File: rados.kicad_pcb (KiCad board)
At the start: 2 copper layers, 83.6 x 106.1 mm, 163 parts, among them J1 CONN_02X03, J10 STEPSTICK, J11 STEPSTICK, J12 STEPSTICK, J13 MICROSD_SLOT_TFP09-2-12B, J2 CONN_02X03, J3 CONN_02X03, J4 STEPSTICK, J5 STEPSTICK, J6 STEPSTICK, J7 CONN_02X03, J8 CONN_02X03, J9 CONN_02X03, P1 CONN_01X02, P10 CONN_01X04, P11 CONN_01X04, P12 CONN_01X04, P13 CONN_02x05, P14 CONN_02x05, P15 CONN_02x07, P16 CONN_01X07, P17 CONN_01X03, P18 CONN_01X03, P19 CONN_01X03, P2 CONN_01X02, P20 CONN_01X03, P21 CONN_02x05, P23 CONN_01X02, P24 CONN_01X02, P25 CONN_01X03, P3 CONN_01X02, P4 CONN_01X02, P5 TERMINAL_BLOCK, P6 TERMINAL_BLOCK, P7 CONN_02X04, P8 CONN_01X04, P9 CONN_01X04, Q1 2N7002P, Q10 2N7002P, Q11 2N7002P, Q12 BC846BPDW1, Q13 BC846BPDW1, Q14 SI2318CDS-T1-GE3, Q15 IRFB7545PbF, Q16 2N7002P, Q17 2N7002P, Q18 BC846BPDW1, Q19 BC846BPDW1, Q2 2N7002P, Q20 SI2318CDS-T1-GE3, Q21 IRFB7545PbF, Q3 2N7002P, Q4 BC846BPDW1, Q5 BC846BPDW1, Q6 BC846BPDW1, Q7 IRFB7545PbF, Q8 SI2318CDS-T1-GE3, Q9 IRFB7545PbF, SW1 BUTTON, U1 ST1S14PHR, U3 ESP-12E

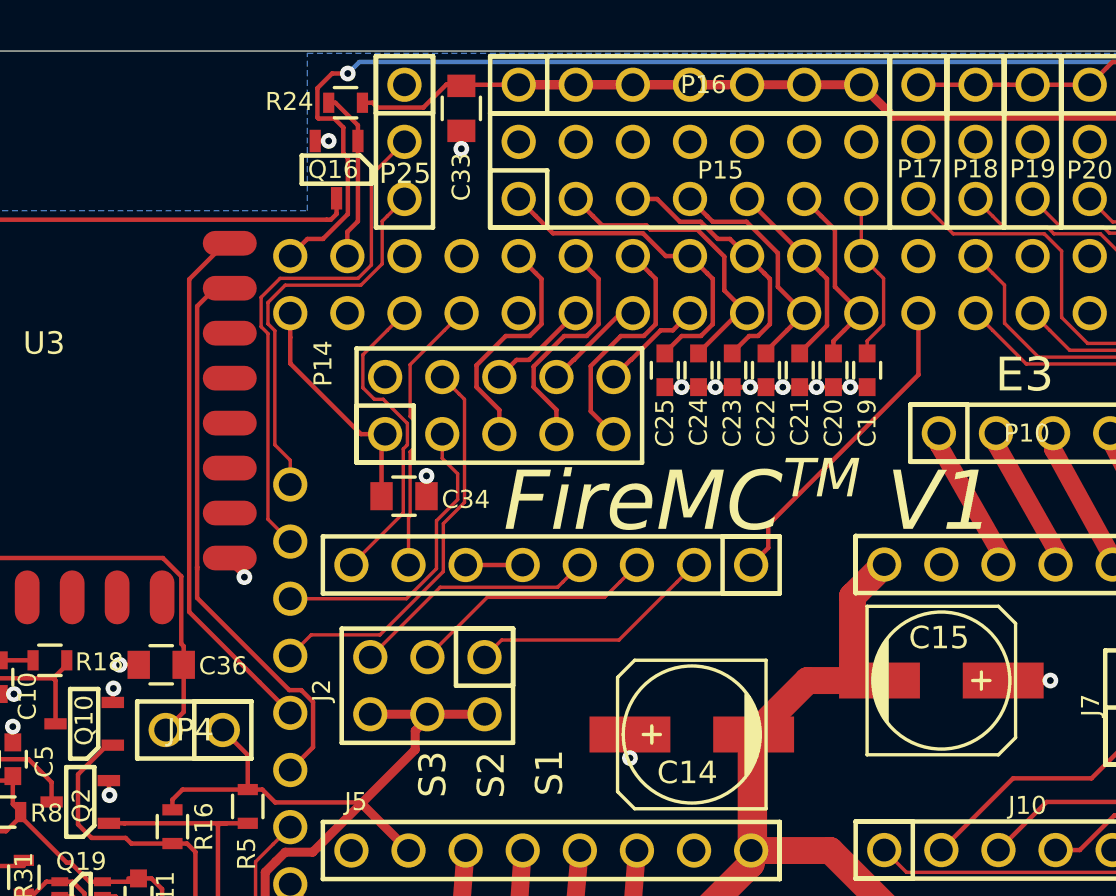
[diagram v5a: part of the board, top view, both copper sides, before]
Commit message: Clearance around wifi power jumper
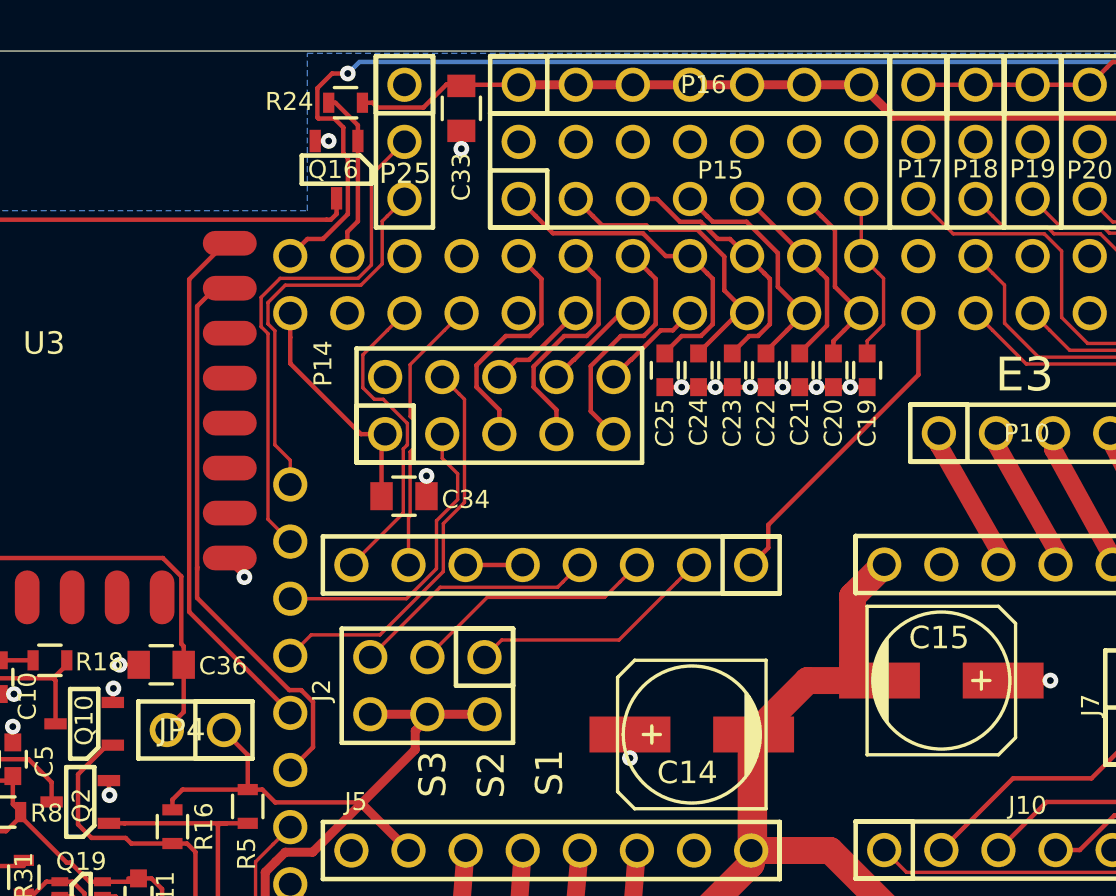
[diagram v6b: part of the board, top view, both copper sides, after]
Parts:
- removed G***: LOGO, logos:OSHW-LOGO
- removed svg2mod (x2): G***, logos:firemc-logo
- removed svg2mod: G***, logos:OtherUseLogo_medium
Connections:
- net Net-(SHIELD1-Pad3V3) renamed Vbuffer
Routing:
- net +3V3: track 474.4 -> 465.9 mm

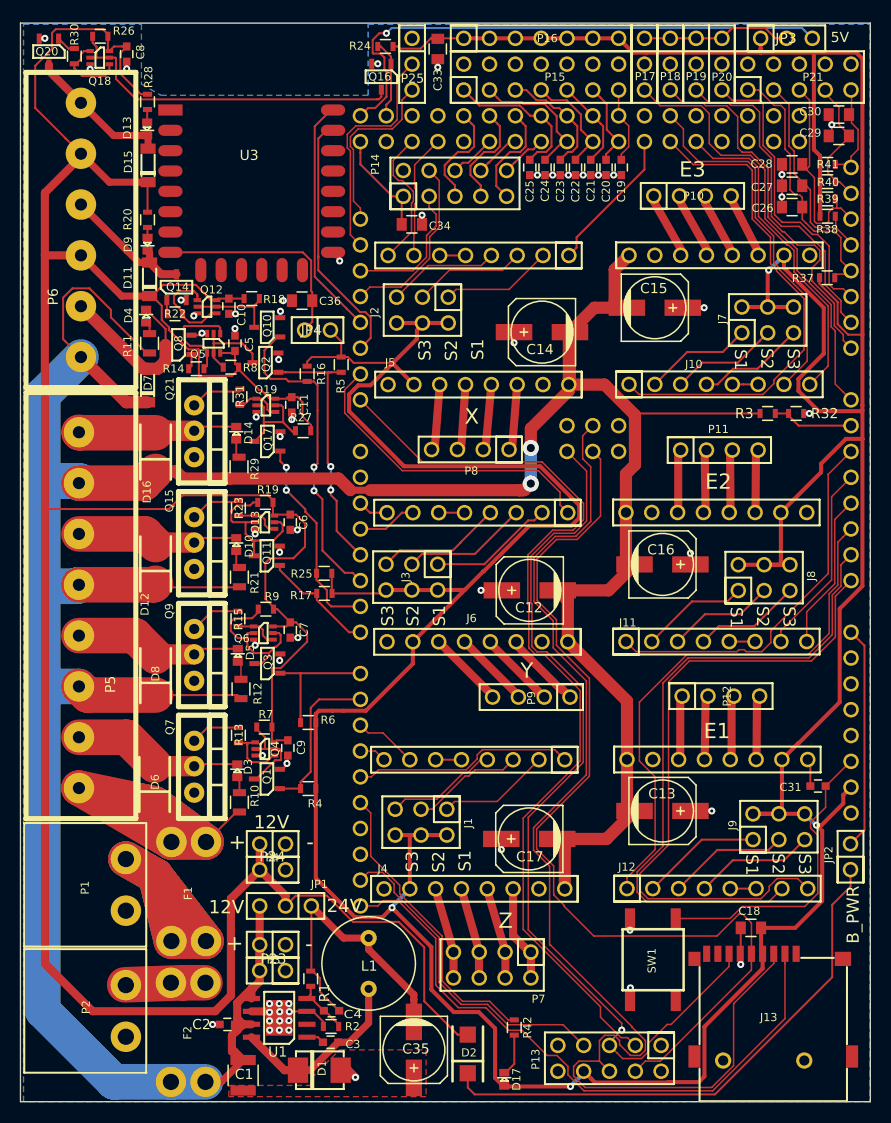
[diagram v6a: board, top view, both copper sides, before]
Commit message: fix analog and wifi
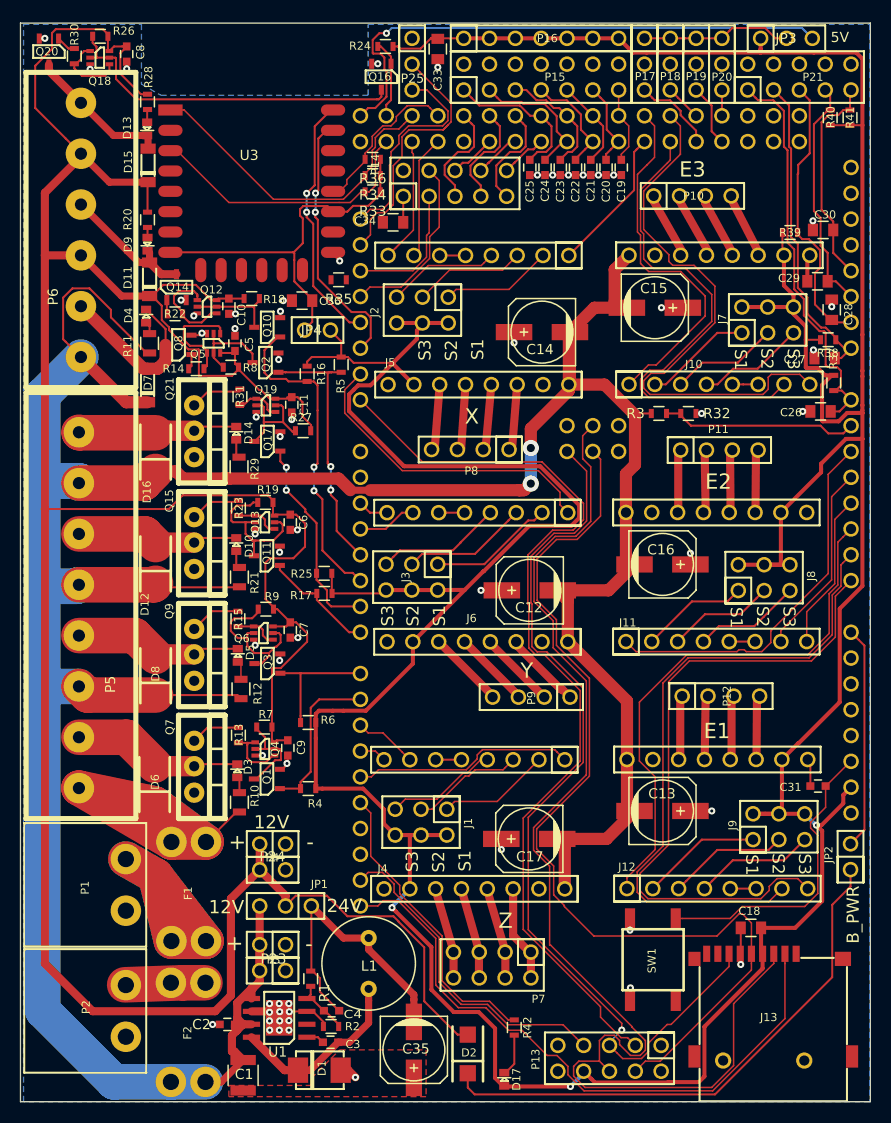
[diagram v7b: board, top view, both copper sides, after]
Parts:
- added R33: 10K, resistors:R_0603, F.Cu at (105.3, 40.5)
- added R34: 10K, resistors:R_0603, F.Cu at (105.3, 38.9)
- added R35: 10K, resistors:R_0603, F.Cu at (102.0, 49.1)
- added R36: 10K, resistors:R_0603, F.Cu at (105.3, 37.3)
- moved C26 20.3 mm to (149.4, 62.1)
- moved C27 17.2 mm to (149.8, 56.9)
- moved C28 14.8 mm to (150.5, 52.1), turned to 90 degrees
- moved C29 14.5 mm to (149.1, 49.3)
- moved R38 12.2 mm to (150.2, 55.0)
- moved C30 11.5 mm to (149.7, 44.2)
- moved R3 10.7 mm to (133.5, 62.3)
- moved R32 10.6 mm to (136.4, 62.3)
- moved R37 10.4 mm to (150.7, 59.3), turned to 270 degrees
- moved R40 6.30 mm to (150.3, 33.2), turned to 90 degrees
- moved R41 5.10 mm to (152.3, 33.2), turned to 90 degrees
- moved R39 4.96 mm to (146.4, 44.5)
- moved C34 1.86 mm to (107.3, 43.5), turned to 180 degrees
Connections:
- C36 pad 1: Net-(C36-Pad1) -> Vesp
- JP4 pad 2: Net-(C36-Pad1) -> Vesp
- SHIELD1 pad 22: Net-(SHIELD1-Pad22) -> ESP-PD
- SHIELD1 pad 25: Net-(SHIELD1-Pad25) -> ESP-RST
- SHIELD1 pad 27: Net-(SHIELD1-Pad27) -> ESP-PROG
- SHIELD1 pad 43: Net-(SHIELD1-Pad43) -> E3-EN
- SHIELD1 pad 44: E3-EN -> E3-STEP
- SHIELD1 pad 45: E3-STEP -> E3-DIR
- SHIELD1 pad 46: E3-DIR -> AUX-1
- SHIELD1 pad 47: Net-(SHIELD1-Pad47) -> AUX-2
- SHIELD1 pad 48: Net-(SHIELD1-Pad48) -> AUX-3
- SHIELD1 pad 49: Net-(SHIELD1-Pad49) -> AUX-4
- SHIELD1 pad AD10: AUX-4 -> T3
- SHIELD1 pad AD11: T0 -> T4
- SHIELD1 pad AD12: T1 -> Net-(SHIELD1-PadAD12)
- SHIELD1 pad AD13: T2 -> Net-(SHIELD1-PadAD13)
- SHIELD1 pad AD14: T3 -> Net-(SHIELD1-PadAD14)
- SHIELD1 pad AD15: T4 -> Net-(SHIELD1-PadAD15)
- SHIELD1 pad AD7: AUX-1 -> T0
- SHIELD1 pad AD8: AUX-2 -> T1
- SHIELD1 pad AD9: AUX-3 -> T2
- U3 pad 1: Net-(U3-Pad1) -> ESP-RST
- U3 pad 17: Net-(U3-Pad17) -> Vesp
- U3 pad 18: Net-(U3-Pad18) -> ESP-PROG
- U3 pad 3: Net-(U3-Pad3) -> ESP-PD
- U3 pad 8: Net-(C36-Pad1) -> Vesp
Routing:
- net Vesp: track 0.00 -> 38.0 mm
- net +3V3: track 465.9 -> 430.3 mm, vias 4 -> 3
- net AUX-1: track 43.1 -> 8.06 mm
- net AUX-2: track 37.4 -> 3.59 mm
- net ESP-RST: track 0.00 -> 32.6 mm
- net ESP-PD: track 0.00 -> 27.7 mm
- net AUX-4: track 29.1 -> 2.54 mm
- net AUX-3: track 32.6 -> 6.13 mm
- net E3-DIR: track 32.2 -> 55.0 mm
- net Net-(C36-Pad1): track 21.4 -> 0.00 mm
- net ESP-PROG: track 0.00 -> 16.6 mm
- net E3-STEP: track 35.8 -> 49.6 mm
- net E3-EN: track 49.2 -> 35.7 mm
- net T0: track 26.7 -> 40.0 mm
- net T4: track 10.2 -> 22.1 mm
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
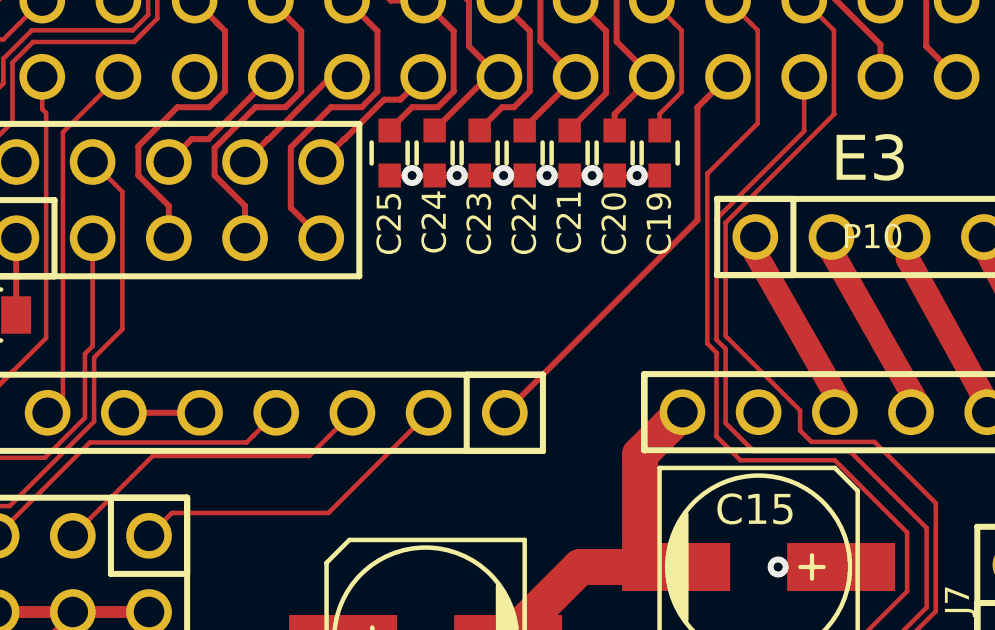
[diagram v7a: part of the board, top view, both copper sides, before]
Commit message: Added logo's that somehow disappeared
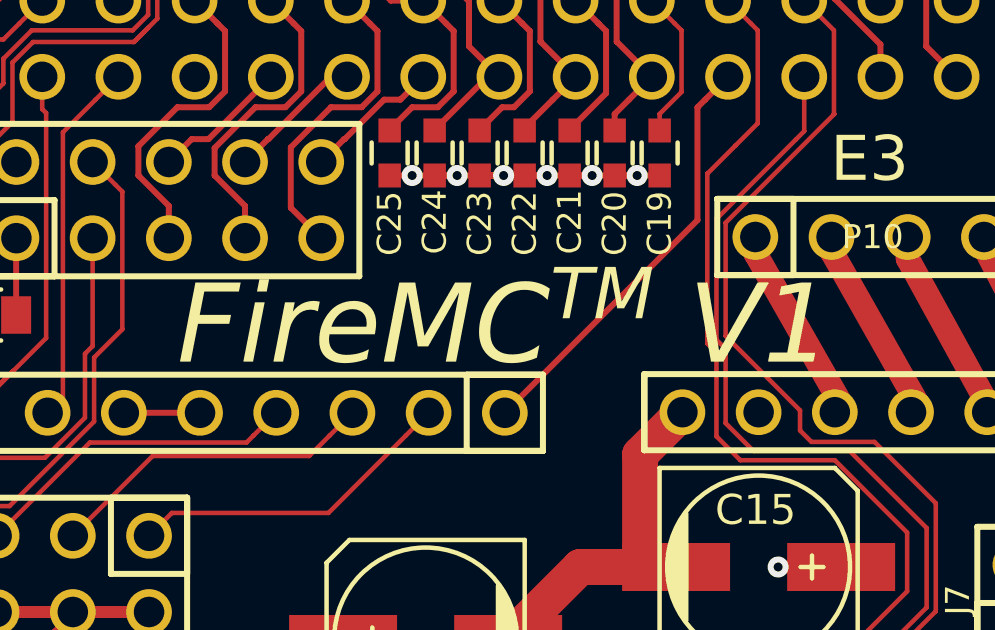
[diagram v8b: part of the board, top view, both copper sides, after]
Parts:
- added G***: LOGO, logos:OSHW-LOGO, B.Cu at (84.0, 55.1)
- added svg2mod: G***, logos:firemc-logo, F.Cu at (124.4, 43.5)
- added svg2mod: G***, logos:firemc-logo, B.Cu at (81.3, 37.5)
- added svg2mod: G***, logos:OtherUseLogo_medium, B.Cu at (91.9, 32.4)
